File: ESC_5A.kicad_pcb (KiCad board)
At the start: 2 copper layers, 62.2 x 25.4 mm, 39 parts, among them IC1 EEPROM, IC2 3.3V Reg, IC3 5V_Reg, IC4 ATSAMD21E17D-AUT, J1 USBc, J2 5V_PWR, J3 M1, J4 M2, J5 PWR_IN, U1 TB67H420FTG_EL

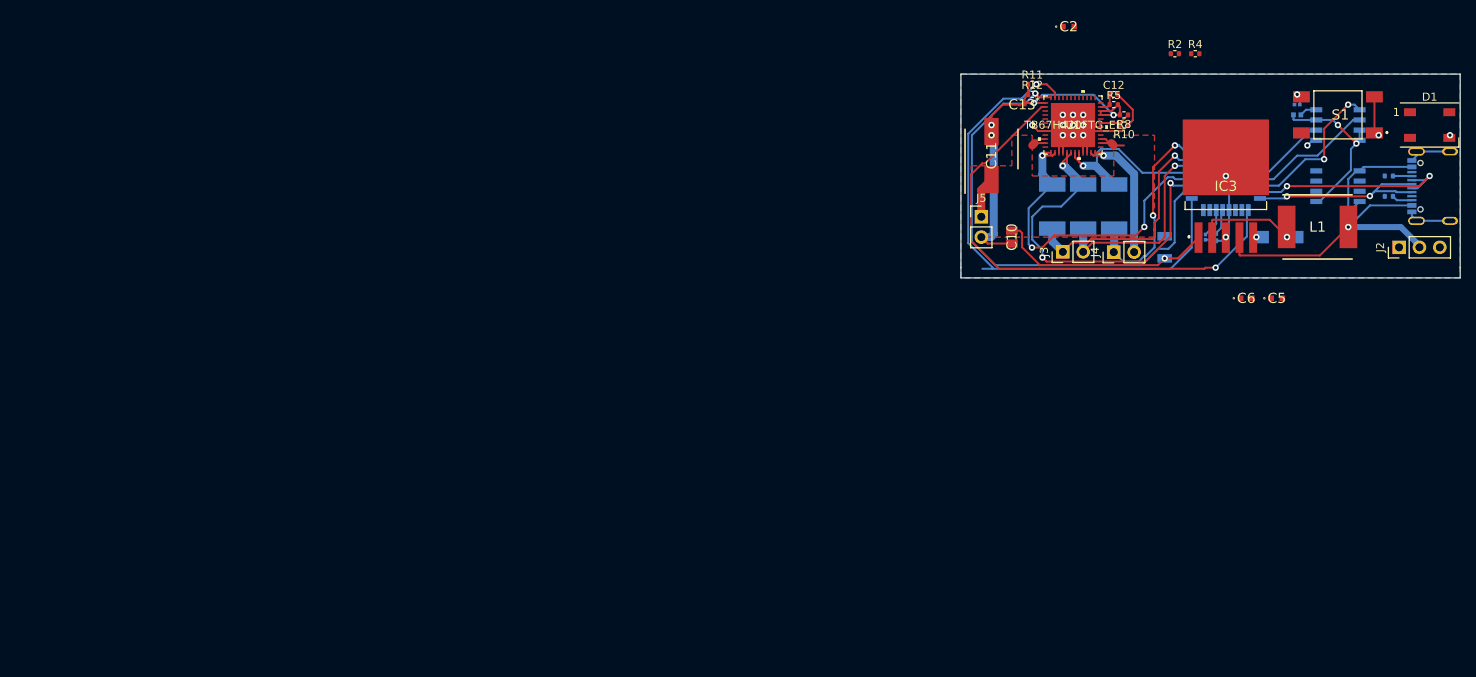
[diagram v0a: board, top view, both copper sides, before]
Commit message: Converted everything to XT30
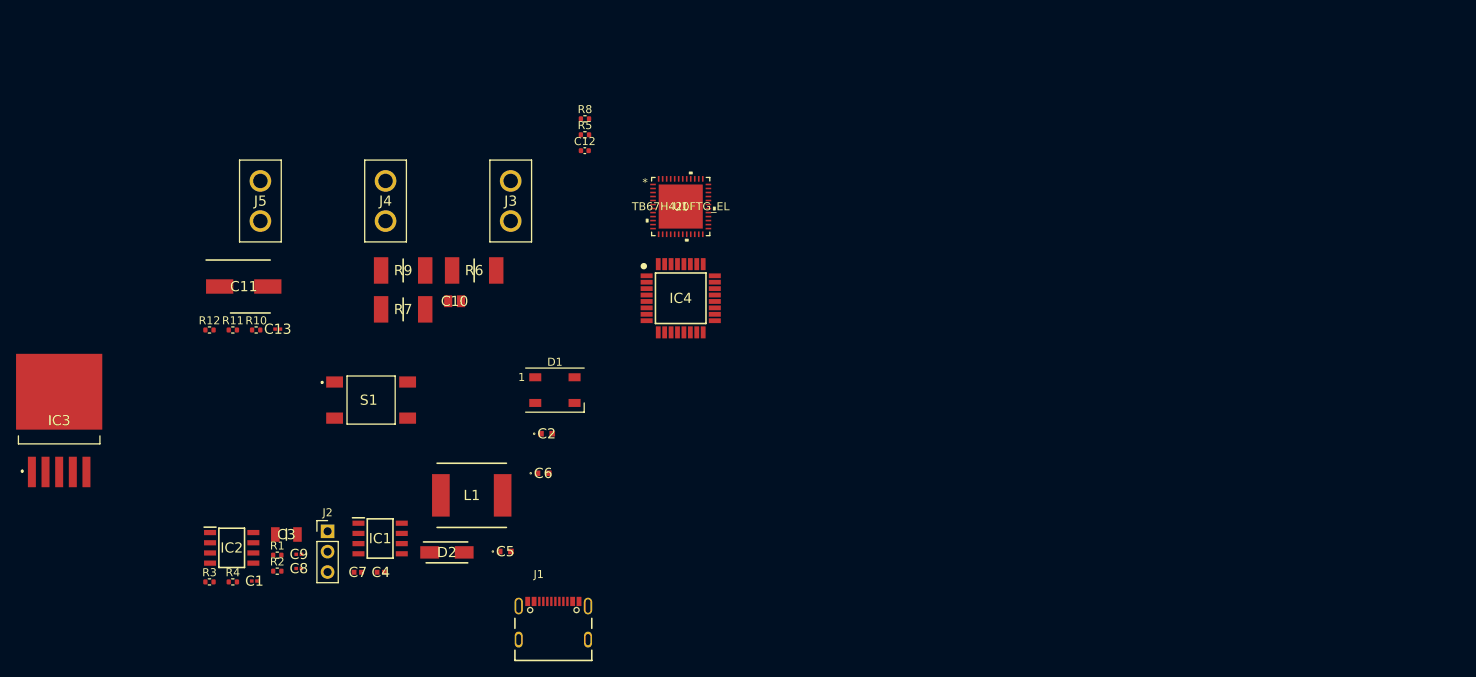
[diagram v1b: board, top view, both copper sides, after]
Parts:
- C1, C3, C4, C7, C8, C9, D2, IC1, IC2, IC4, J1, R1, R3, R6, R7, R9: moved to F.Cu
- J3, J4, J5: footprint Connector_PinHeader_2.54mm:PinHeader_1x02_P2.54mm_Vertical -> SamacSys_Parts:XT30PB
- moved R3 154.7 mm to (123.5, 109.0), turned to 0 degrees
- moved IC3 148.3 mm to (104.8, 88.9)
- moved R1 146.4 mm to (132.0, 105.7), turned to 0 degrees
- moved IC2 145.1 mm to (126.3, 104.8)
- moved C1 142.9 mm to (129.1, 108.9)
- moved J2 138.2 mm to (138.2, 102.7), turned to 0 degrees
- moved R4 136.8 mm to (126.4, 109.0)
- moved IC1 130.0 mm to (144.8, 103.6)
- moved R2 129.1 mm to (132.0, 107.7)
- moved C4 127.7 mm to (144.9, 107.8)
- moved S1 125.6 mm to (143.7, 86.4), turned to 0 degrees
- moved J1 125.2 mm to (166.4, 116.2), turned to 0 degrees
- moved C9 123.9 mm to (134.7, 105.6), turned to 0 degrees
- moved C8 120.3 mm to (134.7, 107.3), turned to 0 degrees
- moved C3 115.2 mm to (133.1, 103.1), turned to 0 degrees
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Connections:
- IC4 pad 27: Net-(IC4-Pad27) -> PPM
- J2 pad 1: Net-(J2-Pad1) -> PPM
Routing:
- net GND: track 98.9 -> 0.00 mm, vias 17 -> 0
- net LO1: track 65.8 -> 0.00 mm, vias 1 -> 0
- net HBMODE: track 61.8 -> 0.00 mm, vias 1 -> 0
- net LO2: track 60.7 -> 0.00 mm, vias 1 -> 0
- net +5V: track 54.6 -> 0.00 mm, vias 1 -> 0
- net ADC_MUX_GND: track 47.9 -> 0.00 mm, vias 3 -> 0
- net ADC_VREFA: track 41.9 -> 0.00 mm, vias 3 -> 0
- net PWR_IN: track 40.9 -> 0.00 mm, vias 1 -> 0
- net ADC_1: track 29.3 -> 0.00 mm, vias 1 -> 0
- net D-: track 27.3 -> 0.00 mm, vias 2 -> 0
- net ADC_VREFB: track 26.1 -> 0.00 mm, vias 1 -> 0
- net ADC_2: track 25.8 -> 0.00 mm, vias 2 -> 0
- net ADC_3: track 25.4 -> 0.00 mm, vias 1 -> 0
- net D+: track 25.2 -> 0.00 mm, vias 2 -> 0
- net TBLKAB: track 23.5 -> 0.00 mm, vias 2 -> 0
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- removed copper zone on B.Cu, net GND
- removed copper zone on F.Cu, net PWR_IN
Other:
- board outline removed

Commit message: testing other options
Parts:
- IC4, J1: moved to B.Cu
- L1: footprint SamacSys_Parts:INDM8680X300N -> SamacSys_Parts:XAL6060333MEC
- moved J3 110.3 mm to (50.8, 55.9)
- moved J4 102.2 mm to (43.8, 48.3), turned to 90 degrees
- moved J5 86.7 mm to (43.2, 55.9)
- moved J2 71.1 mm to (201.3, 69.8)
- moved D2 60.6 mm to (109.2, 63.5), turned to 90 degrees
- moved IC3 52.8 mm to (64.1, 55.2)
- moved U1 38.0 mm to (146.1, 73.7)
- moved IC4 36.2 mm to (146.1, 73.7)
- moved D1 32.9 mm to (139.7, 104.1)
- moved C2 32.0 mm to (139.1, 108.6)
- moved J1 30.9 mm to (156.2, 87.0), turned to 180 degrees
- moved S1 30.4 mm to (133.3, 114.9)
- moved C5 29.7 mm to (134.1, 91.4)
- moved R7 28.8 mm to (174.0, 63.5), turned to 90 degrees
- moved R9 28.1 mm to (171.4, 55.2), turned to 270 degrees
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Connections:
- IC4 pad 12: INA1 -> INB2
- IC4 pad 13: INA2 -> INB1
- IC4 pad 14: INB1 -> INA2
- IC4 pad 15: INB2 -> INA1
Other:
- board outline added: 31.1 x 21 mm

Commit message: Pre_layout
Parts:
- J3, J4, J5: footprint SamacSys_Parts:XT30PB -> Connector_AMASS:AMASS_XT30U-M_1x02_P5.0mm_Vertical
- moved J2 187.4 mm to (14.0, 74.9), turned to 180 degrees
- moved J1 144.5 mm to (14.0, 61.6), turned to 90 degrees
- moved R9 112.3 mm to (62.9, 26.7)
- moved IC4 103.7 mm to (46.4, 102.2)
- moved U1 103.7 mm to (46.4, 102.2)
- moved R7 102.2 mm to (72.4, 74.3)
- moved R6 102.2 mm to (67.3, 74.3)
- moved C11 79.8 mm to (56.5, 85.1)
- moved S1 75.9 mm to (57.8, 122.6)
- moved C10 71.9 mm to (70.6, 105.4)
- moved C13 71.9 mm to (85.0, 99.7)
- moved R10 71.9 mm to (82.3, 99.8)
- moved R11 71.9 mm to (79.4, 99.8)
- moved R12 71.9 mm to (76.5, 99.8)
- moved R5 71.9 mm to (91.6, 95.2)
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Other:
- board outline removed

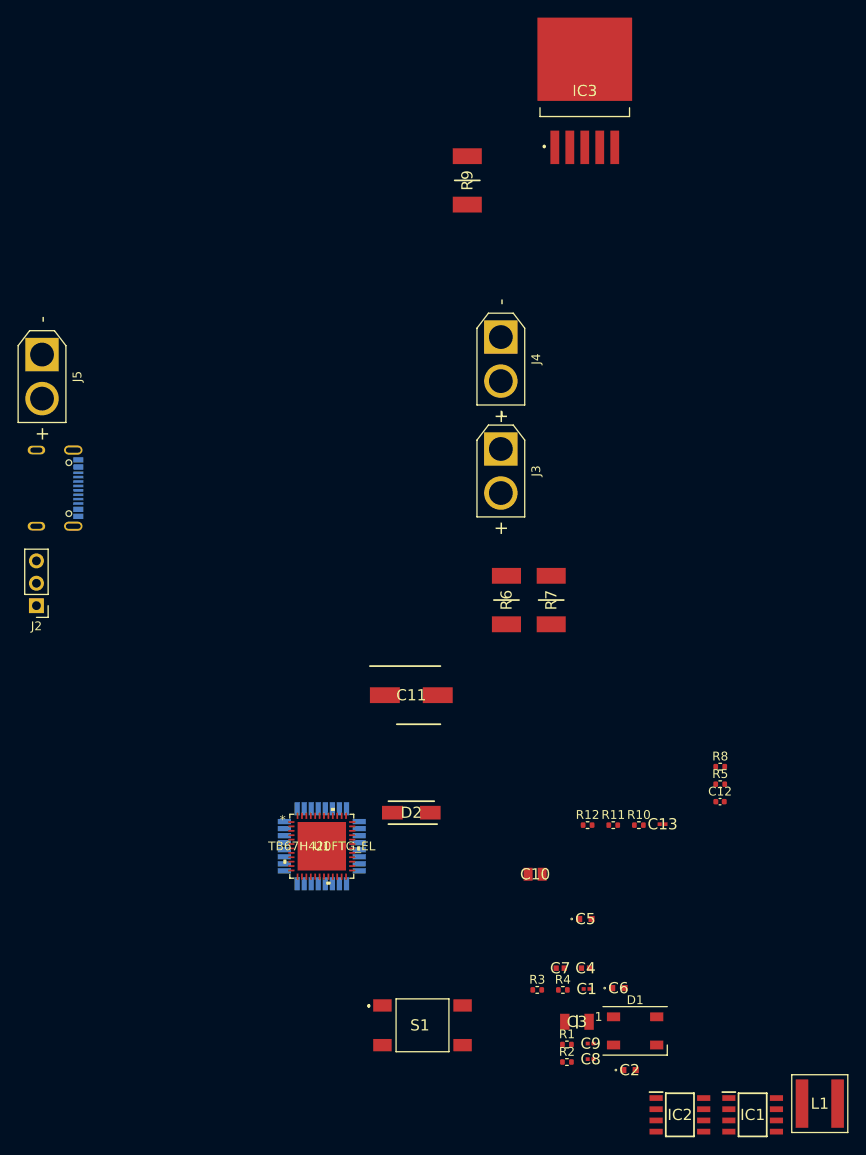
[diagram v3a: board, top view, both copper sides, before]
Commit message: Was able to shrink board another 6mm
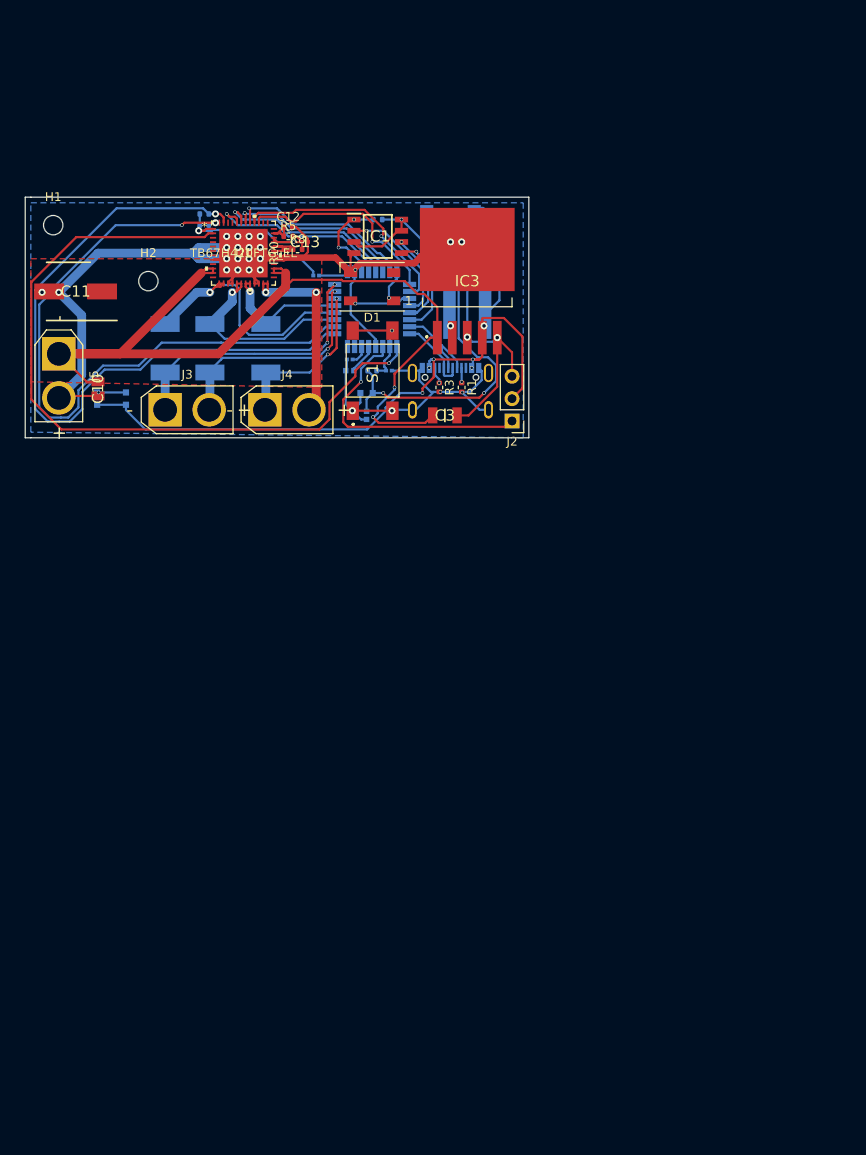
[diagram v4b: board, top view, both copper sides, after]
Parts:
- added H1: MountingHole, MountingHole:MountingHole_2.2mm_M2, F.Cu at (15.9, 31.8)
- added H2: MountingHole, MountingHole:MountingHole_2.2mm_M2, F.Cu at (26.7, 38.1)
- C1, C2, C4, C5, C6, C7, C8, C9, D2, IC2, L1, R11, R12, R2, R4, R6, R7, R9: moved to B.Cu
- moved IC1 108.4 mm to (52.7, 33.0)
- moved IC2 104.3 mm to (61.0, 31.7)
- moved L1 98.1 mm to (62.9, 41.9)
- moved C9 92.6 mm to (45.7, 37.5)
- moved R4 89.9 mm to (52.7, 31.1), turned to 180 degrees
- moved D1 89.6 mm to (52.1, 38.7), turned to 180 degrees
- moved C6 89.3 mm to (20.9, 51.4), turned to 90 degrees
- moved C8 84.0 mm to (49.5, 47.0)
- moved R11 83.5 mm to (33.0, 30.5)
- moved C2 82.4 mm to (51.4, 50.8), turned to 180 degrees
- moved C12 81.6 mm to (42.5, 31.9)
- moved R2 81.5 mm to (52.1, 48.3)
- moved R12 80.8 mm to (33.0, 31.8)
- moved R5 79.2 mm to (42.5, 33.0)
- moved C5 78.8 mm to (24.1, 51.4), turned to 90 degrees
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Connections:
- IC4 pad 6: ADC_3 -> ADC_2
- IC4 pad 7: ADC_1 -> ADC_3
- IC4 pad 8: ADC_2 -> ADC_1
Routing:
- net GND: track 0.00 -> 217.8 mm, vias 0 -> 28
- net PWR_IN: track 0.00 -> 105.2 mm, vias 0 -> 2
- net +5V: track 0.00 -> 90.3 mm, vias 0 -> 6
- net HBMODE: track 0.00 -> 85.1 mm, vias 0 -> 1
- net LO1: track 0.00 -> 79.6 mm, vias 0 -> 1
- net LO2: track 0.00 -> 76.4 mm, vias 0 -> 2
- net +3V3: track 0.00 -> 55.3 mm, vias 0 -> 3
- net ADC_1: track 0.00 -> 31.4 mm, vias 0 -> 2
- net PPM: track 0.00 -> 31.2 mm, vias 0 -> 1
- net ADC_VREFA: track 0.00 -> 29.9 mm, vias 0 -> 1
- net PWMB: track 0.00 -> 26.6 mm, vias 0 -> 1
- net ADC_3: track 0.00 -> 25.8 mm, vias 0 -> 2
- net ADC_MUX_GND: track 0.00 -> 23.9 mm, vias 0 -> 1
- net PWMA: track 0.00 -> 23.8 mm, vias 0 -> 1
- net MotorB_Neg: track 0.00 -> 22.0 mm, vias 0 -> 2
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- added copper zone on B.Cu, net GND
- added copper zone on F.Cu, net PWR_IN
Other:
- board outline added: 57.1 x 27.3 mm

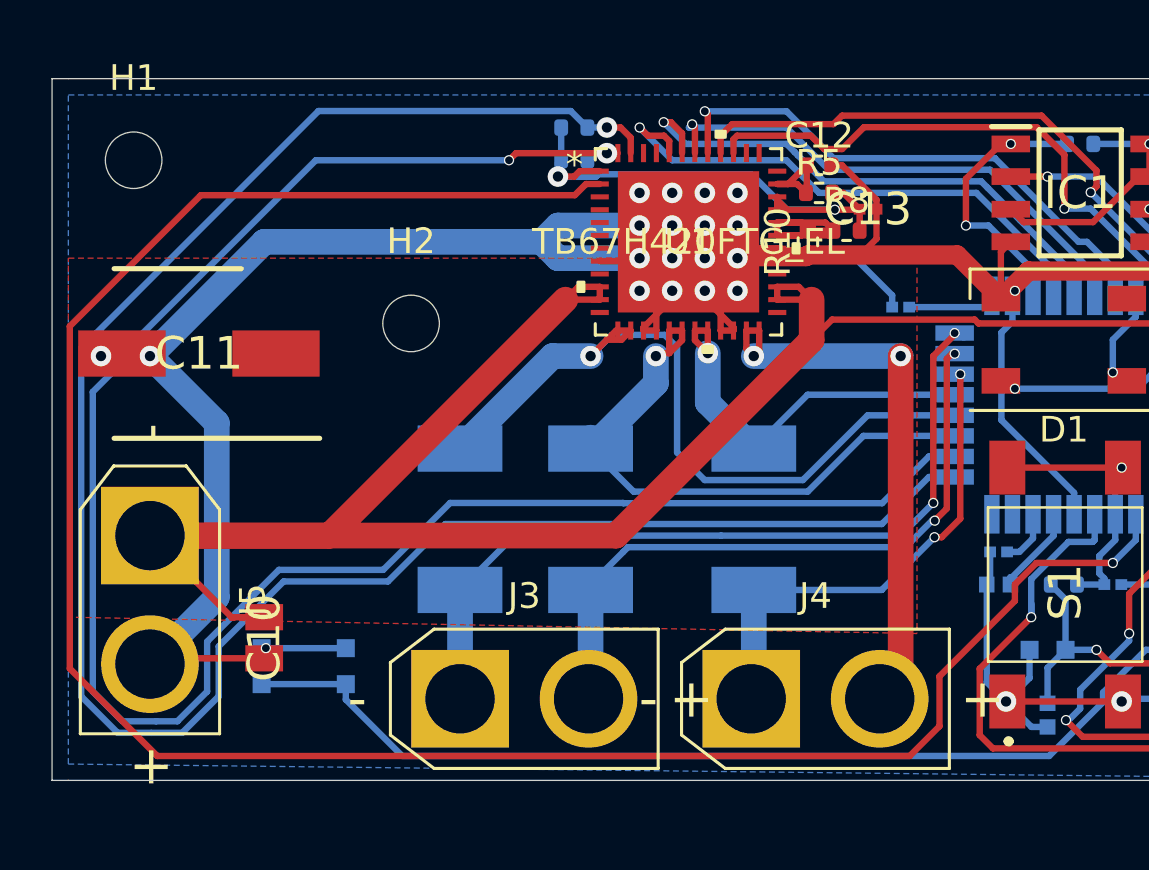
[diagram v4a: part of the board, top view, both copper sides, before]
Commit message: Added second PPM input for indepedant motor control
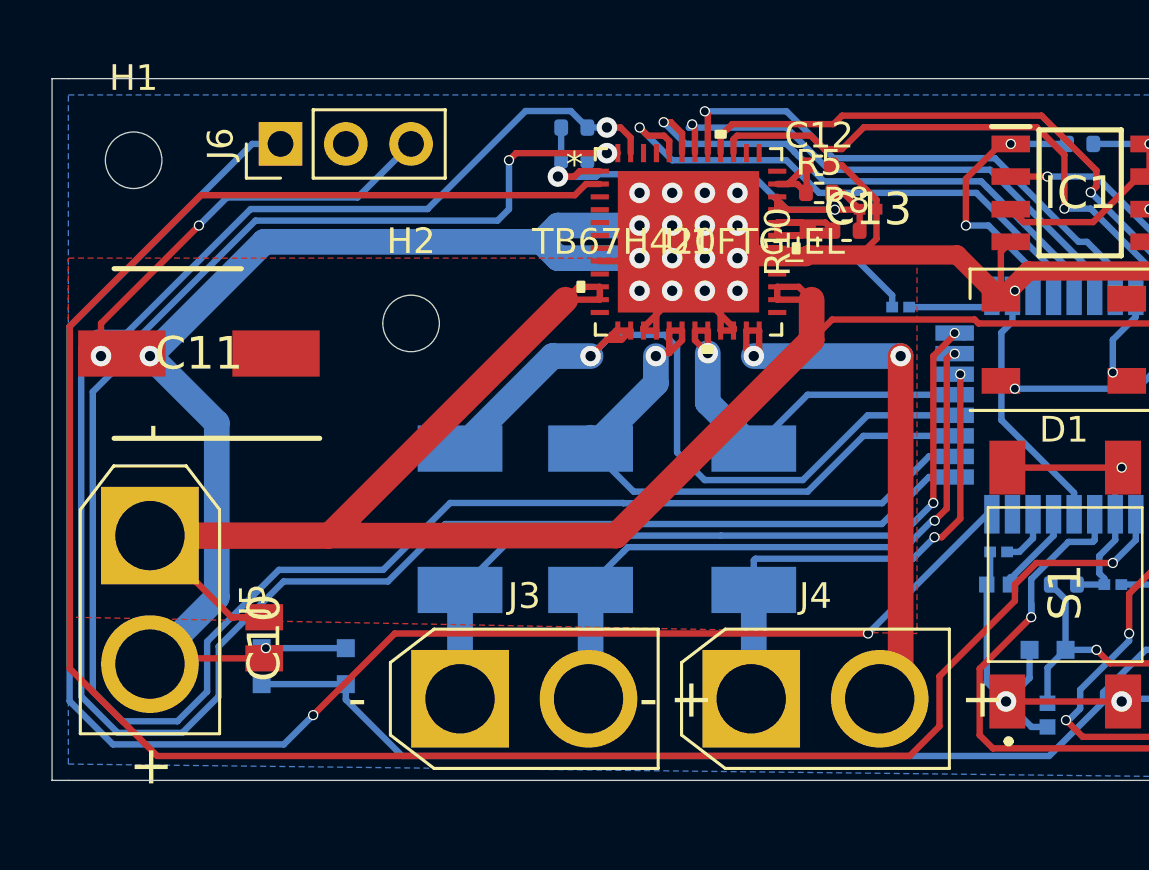
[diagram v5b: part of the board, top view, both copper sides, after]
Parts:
- added J6: 5V_PWR, Connector_PinHeader_2.54mm:PinHeader_1x03_P2.54mm_Vertical, F.Cu at (21.6, 31.1)
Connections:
- net PPM renamed PPM_1
- IC4 pad 32: Net-(IC4-Pad32) -> PPM_2
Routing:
- net PPM_2: track 0.00 -> 66.0 mm, vias 0 -> 2
- net GND: track 217.8 -> 234.0 mm, vias 28 -> 29
- net LO2: track 76.4 -> 77.6 mm
- net ADC_2: track 19.3 -> 19.9 mm
